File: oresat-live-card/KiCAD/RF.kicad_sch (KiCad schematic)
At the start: 36 parts, among them J5 2X1_TH_JUMPEP, J9 Conn_Coaxial, U19 TQP9111, U6 SN74LVC1G32QDBVRQ1, U8 MIC94090YC6-TR

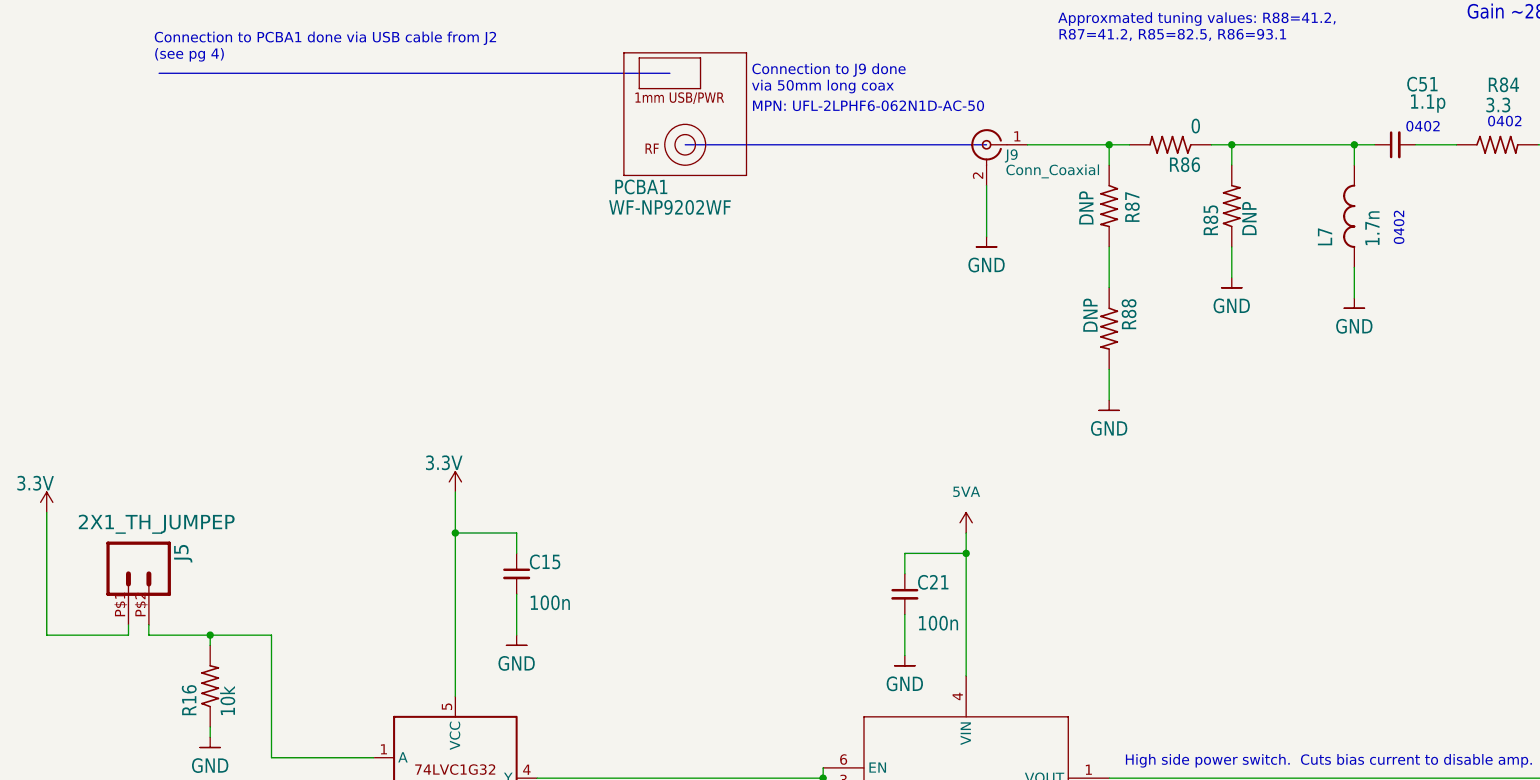
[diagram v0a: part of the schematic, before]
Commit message: Finished layout, and cleaned up more errors/warnings
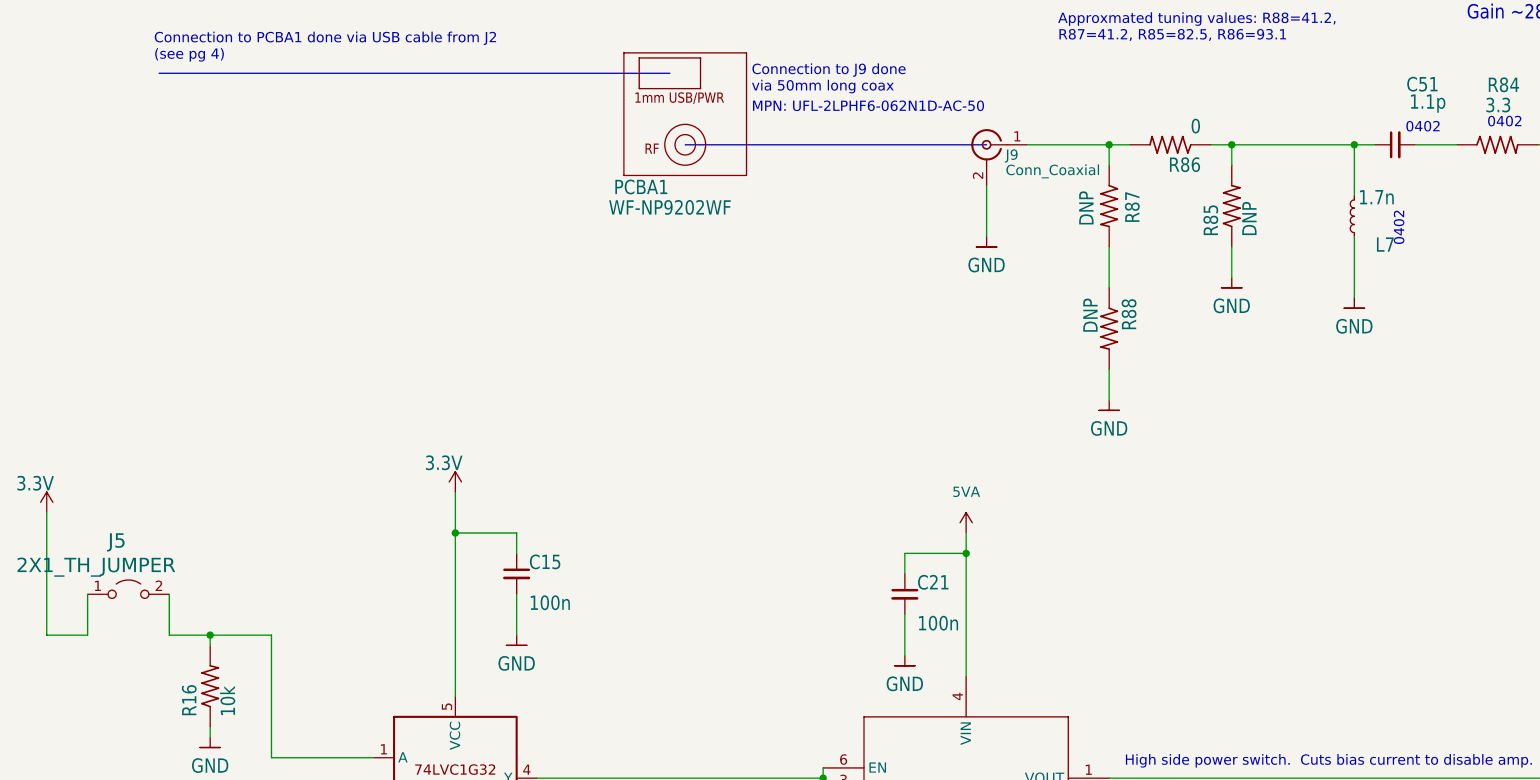
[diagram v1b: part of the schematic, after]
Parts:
- J5: value 2X1_TH_JUMPEP -> 2X1_TH_JUMPER; symbol oresat-live-card-eagle-import:2X1_TH_JUMPEP -> Jumper:Jumper_2_Open
- L7: symbol oresat-live-card-eagle-import:L-US0402-C-NOSILK -> Device:L_Small
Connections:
- net 3.3V: now also J5.1 (A); no longer J5.P$1 (1)
- net at R16.2, U6.1 (A): now also J5.2 (B); no longer J5.P$2 (2)
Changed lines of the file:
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@@
     (stroke (width 0) (type default))
   )
-  (wire (pts (xy 205.74 129.54) (xy 205.74 133.35))
+  (wire (pts (xy 205.74 125.73) (xy 205.74 133.35))
     (stroke (width 0) (type default))
   )
@@
     (stroke (width 0) (type default))
   )
-  (wire (pts (xy 205.74 116.84) (xy 205.74 114.3))
+  (wire (pts (xy 205.74 114.3) (xy 205.74 120.65))
     (stroke (width 0) (type default))
   )
@@
     (stroke (width 0) (type default))
   )
-  (wire (pts (xy 55.88 173.99) (xy 55.88 175.26))
+  (wire (pts (xy 58.42 170.18) (xy 58.42 175.26))
     (stroke (width 0) (type default))
   )
@@
     (stroke (width 0) (type default))
   )
-  (wire (pts (xy 55.88 175.26) (xy 63.5 175.26))
+  (wire (pts (xy 58.42 175.26) (xy 63.5 175.26))
     (stroke (width 0) (type default))
   )
@@
     (stroke (width 0) (type default))
   )
-  (wire (pts (xy 53.34 175.26) (xy 43.18 175.26))
-    (stroke (width 0) (type default))
-  )
-  (wire (pts (xy 53.34 173.99) (xy 53.34 175.26))
+  (wire (pts (xy 48.26 175.26) (xy 43.18 175.26))
+    (stroke (width 0) (type default))
+  )
+  (wire (pts (xy 48.26 170.18) (xy 48.26 175.26))
     (stroke (width 0) (type default))
   )
@@
     )
   )
-  (symbol (lib_id "oresat-live-card-eagle-import:2X1_TH_JUMPEP") (at 53.34 166.37 270) (unit 1)
-    (in_bom yes) (on_board yes) (dnp no)
-    (property "Reference" "J5" (at 58.928 163.83 0)
+  (symbol (lib_id "Jumper:Jumper_2_Open") (at 53.34 170.18 0) (unit 1)
+    (in_bom yes) (on_board yes) (dnp no)
+    (property "Reference" "J5" (at 50.8 164.592 0)
       (effects (font (size 1.778 1.778)) (justify left bottom))
     )
-    (property "Value" "2X1_TH_JUMPEP" (at 46.99 162.306 90)
+    (property "Value" "2X1_TH_JUMPER" (at 39.37 167.64 0)
       (effects (font (size 1.778 1.778)) (justify left bottom))
     )
-    (property "Footprint" "oresat-live-card:2X1" (at 53.34 166.37 0)
-      (effects (font (size 1.27 1.27)) hide)
-    )
-    (property "Datasheet" "" (at 53.34 166.37 0)
-      (effects (font (size 1.27 1.27)) hide)
-    )
-    (pin "P$1")
-    (pin "P$2")
+    (property "Footprint" "oresat-live-card:2X1" (at 53.34 170.18 0)
+      (effects (font (size 1.27 1.27)) hide)
+    )
+    (property "Datasheet" "" (at 53.34 170.18 0)
+      (effects (font (size 1.27 1.27)) hide)
+    )
+    (pin "1")
+    (pin "2")
     (instances
       (project "oresat-live-card"
@@
     )
   )
-  (symbol (lib_id "oresat-live-card-eagle-import:L-US0402-C-NOSILK") (at 205.74 121.92 90) (unit 1)
-    (in_bom yes) (on_board yes) (dnp no)
-    (property "Reference" "L7" (at 203.2 127 0)
-      (effects (font (size 1.778 1.5113)) (justify left bottom))
-    )
-    (property "Value" "1.7n" (at 207.01 127 0)
+  (symbol (lib_id "Device:L_Small") (at 205.74 123.19 180) (unit 1)
+    (in_bom yes) (on_board yes) (dnp no)
+    (property "Reference" "L7" (at 210.82 125.73 0)
+      (effects (font (size 1.778 1.5113)) (justify left bottom))
+    )
+    (property "Value" "1.7n" (at 210.82 121.92 0)
       (effects (font (size 1.778 1.5113)) (justify left top))
     )
-    (property "Footprint" "Resistor_SMD:R_0402_1005Metric" (at 205.74 121.92 0)
-      (effects (font (size 1.27 1.27)) hide)
-    )
-    (property "Datasheet" "" (at 205.74 121.92 0)
-      (effects (font (size 1.27 1.27)) hide)
-    )
-    (property "Value" "0402DC-1N7XJRU" (at 205.74 121.92 0)
+    (property "Footprint" "Resistor_SMD:R_0402_1005Metric" (at 205.74 123.19 0)
+      (effects (font (size 1.27 1.27)) hide)
+    )
+    (property "Datasheet" "" (at 205.74 123.19 0)
+      (effects (font (size 1.27 1.27)) hide)
+    )
+    (property "Value" "0402DC-1N7XJRU" (at 205.74 123.19 0)
       (effects (font (size 1.778 1.5113)) (justify left bottom) hide)
     )
-    (property "Description" "1.7nH RF Inductor, ceramic core, 5% tol" (at 205.74 121.92 0)
-      (effects (font (size 1.27 1.27)) hide)
-    )
-    (property "Distributor" "DigiKey" (at 205.74 121.92 0)
-      (effects (font (size 1.27 1.27)) hide)
-    )
-    (property "MPN" "0402DC-1N7XJRU" (at 205.74 121.92 0)
-      (effects (font (size 1.27 1.27)) hide)
-    )
+    (property "Description" "1.7nH RF Inductor, ceramic core, 5% tol" (at 205.74 123.19 0)
+      (effects (font (size 1.27 1.27)) hide)
+    )
+    (property "Distributor" "DigiKey" (at 205.74 123.19 0)
+      (effects (font (size 1.27 1.27)) hide)
+    )
+    (property "MPN" "0402DC-1N7XJRU" (at 205.74 123.19 0)
+      (effects (font (size 1.27 1.27)) hide)
+    )

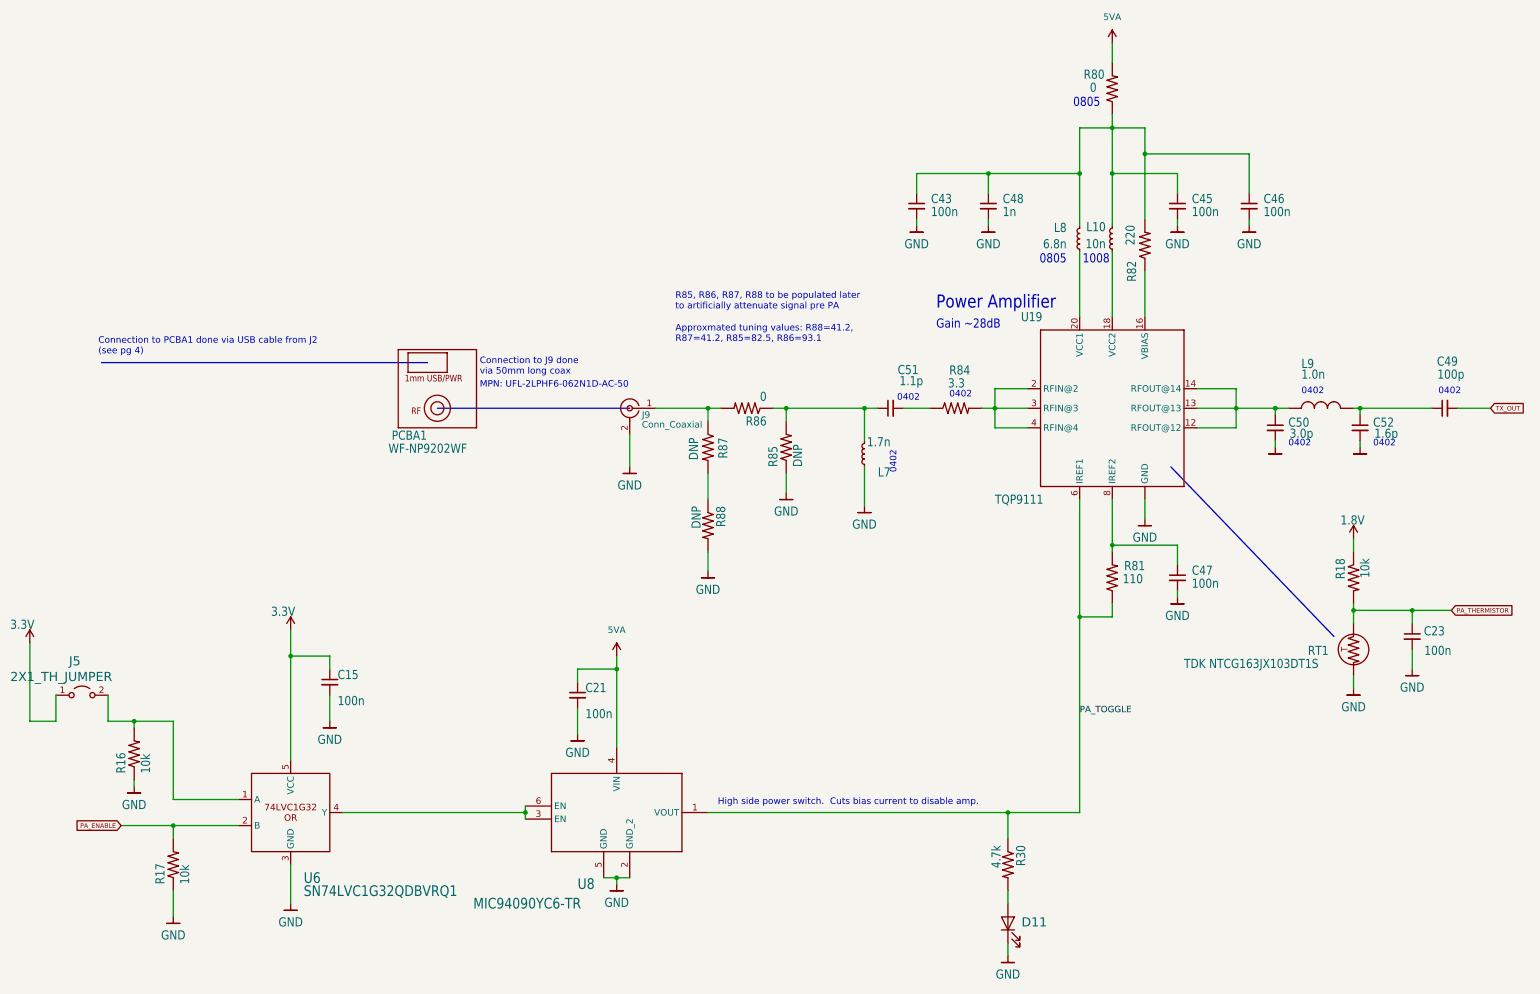
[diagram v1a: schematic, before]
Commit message: Cleaned up ERC and DRC errors on DxWiFi Card
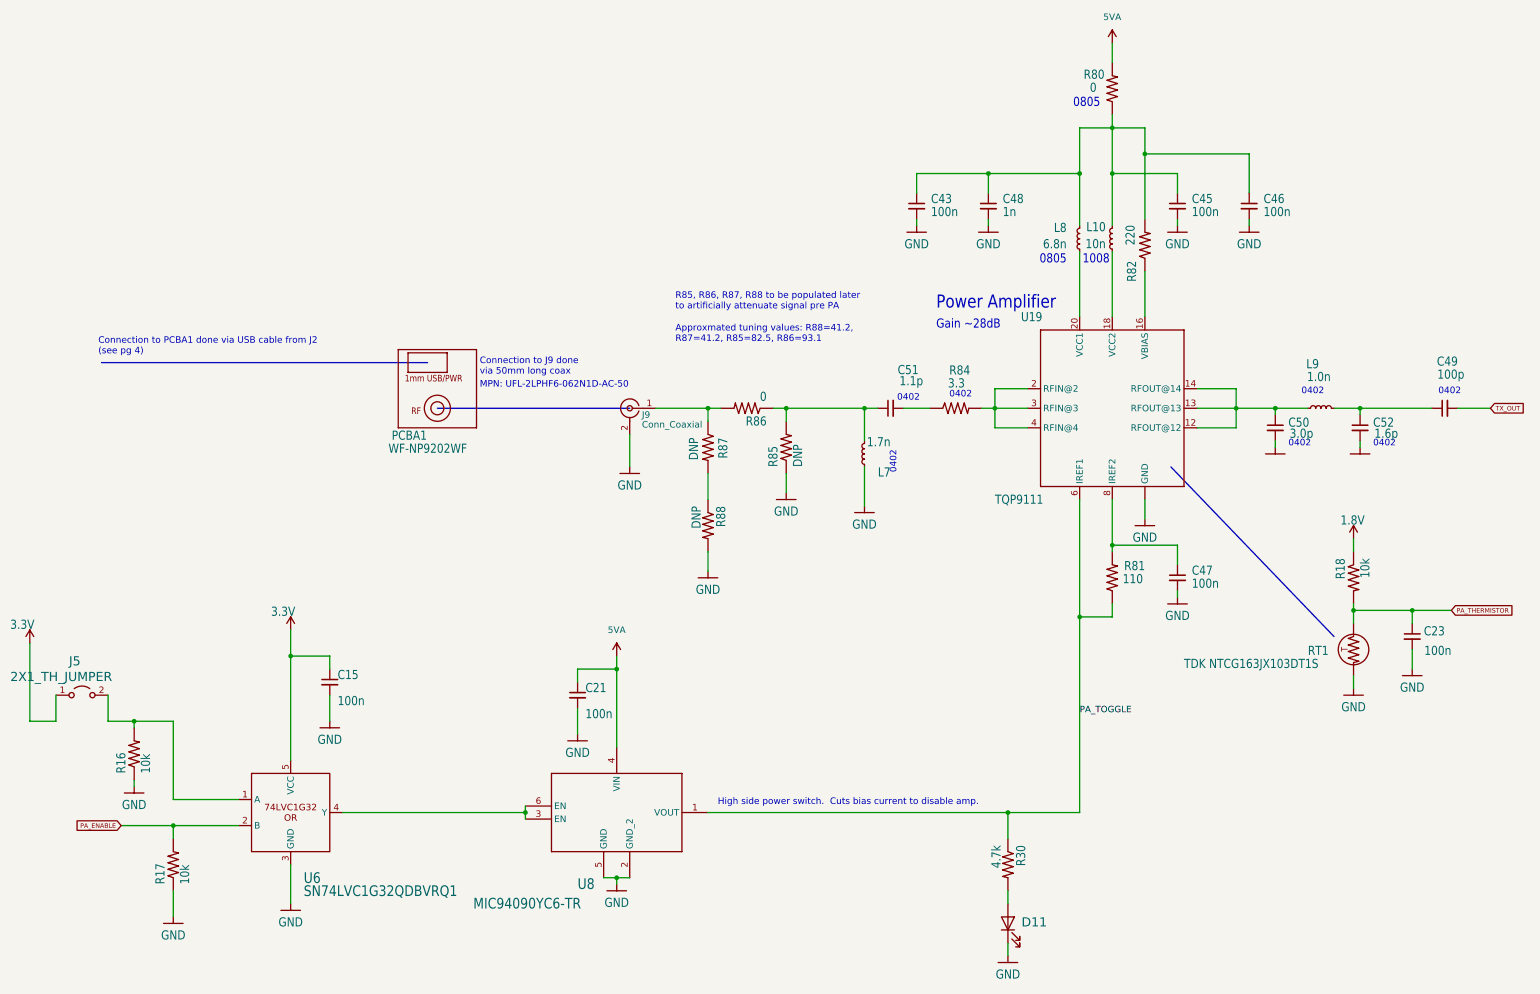
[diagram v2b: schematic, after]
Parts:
- L9: symbol oresat-live-card-eagle-import:L-US0402-C-NOSILK -> Device:L_Small
- RT1: symbol oresat-live-card-eagle-import:THERMISTOR--0603-THERMISTOR-B -> oresat-passives:THERMISTOR
- U8: symbol oresat-live-card-eagle-import:MIC94090YC6-TR -> oresat-ics:MIC94090YC6-TR
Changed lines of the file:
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@@
     (stroke (width 0) (type default))
   )
-  (wire (pts (xy 300.99 114.3) (xy 302.26 114.3))
+  (wire (pts (xy 297.18 114.3) (xy 302.26 114.3))
     (stroke (width 0) (type default))
   )
@@
     (stroke (width 0) (type default))
   )
-  (wire (pts (xy 285.75 114.3) (xy 288.29 114.3))
+  (wire (pts (xy 285.75 114.3) (xy 292.1 114.3))
     (stroke (width 0) (type default))
   )
@@
     )
   )
-  (symbol (lib_id "oresat-live-card-eagle-import:THERMISTOR--0603-THERMISTOR-B") (at 300.99 161.29 90) (mirror x) (unit 1)
+  (symbol (lib_id "oresat-passives:THERMISTOR") (at 300.99 161.29 90) (mirror x) (unit 1)
     (in_bom yes) (on_board yes) (dnp no)
     (property "Reference" "RT1" (at 292.1 162.56 90)
@@
     )
   )
-  (symbol (lib_id "oresat-live-card-eagle-import:L-US0402-C-NOSILK") (at 295.91 114.3 0) (unit 1)
-    (in_bom yes) (on_board yes) (dnp no)
-    (property "Reference" "L9" (at 290.83 106.68 0)
-      (effects (font (size 1.778 1.5113)) (justify left bottom))
-    )
-    (property "Value" "1.0n" (at 290.83 106.68 0)
+  (symbol (lib_id "Device:L_Small") (at 294.64 114.3 90) (unit 1)
+    (in_bom yes) (on_board yes) (dnp no)
+    (property "Reference" "L9" (at 294.259 104.648 90)
+      (effects (font (size 1.778 1.5113)) (justify left bottom))
+    )
+    (property "Value" "1.0n" (at 296.545 109.22 90)
       (effects (font (size 1.778 1.5113)) (justify left top))
     )
-    (property "Footprint" "Resistor_SMD:R_0402_1005Metric" (at 295.91 114.3 0)
-      (effects (font (size 1.27 1.27)) hide)
-    )
-    (property "Datasheet" "" (at 295.91 114.3 0)
-      (effects (font (size 1.27 1.27)) hide)
-    )
-    (property "Value" "MLK1005S1N0ST000" (at 295.91 114.3 0)
-      (effects (font (size 1.778 1.5113)) (justify left bottom) hide)
-    )
-    (property "Description" "FIXED IND 1NH 500MA 100 MOHM SMD" (at 295.91 114.3 0)
-      (effects (font (size 1.27 1.27)) hide)
-    )
-    (property "Distributor" "DigiKey" (at 295.91 114.3 0)
-      (effects (font (size 1.27 1.27)) hide)
-    )
-    (property "MPN" "MLK1005S1N0ST000" (at 295.91 114.3 0)
+    (property "Footprint" "Resistor_SMD:R_0402_1005Metric" (at 294.64 114.3 0)
+      (effects (font (size 1.27 1.27)) hide)
+    )
+    (property "Datasheet" "" (at 294.64 114.3 0)
+      (effects (font (size 1.27 1.27)) hide)
+    )
+    (property "Value" "MLK1005S1N0ST000" (at 294.64 114.3 0)
+      (effects (font (size 1.778 1.5113)) (justify left bottom) hide)
+    )
+    (property "Description" "FIXED IND 1NH 500MA 100 MOHM SMD" (at 294.64 114.3 0)
+      (effects (font (size 1.27 1.27)) hide)
+    )
+    (property "Distributor" "DigiKey" (at 294.64 114.3 0)
+      (effects (font (size 1.27 1.27)) hide)
+    )
+    (property "MPN" "MLK1005S1N0ST000" (at 294.64 114.3 0)
       (effects (font (size 1.27 1.27)) hide)
     )
@@
     )
   )
-  (symbol (lib_id "oresat-live-card-eagle-import:MIC94090YC6-TR") (at 157.48 193.04 0) (mirror y) (unit 1)
+  (symbol (lib_id "oresat-ics:MIC94090YC6-TR") (at 157.48 193.04 0) (mirror y) (unit 1)
     (in_bom yes) (on_board yes) (dnp no)
     (property "Reference" "U8" (at 149.86 205.74 0)
